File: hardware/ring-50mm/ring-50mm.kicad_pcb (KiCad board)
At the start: 2 copper layers, 50.2 x 56.6 mm, 53 parts, among them J1 Conn_01x03, J2 Conn_01x03

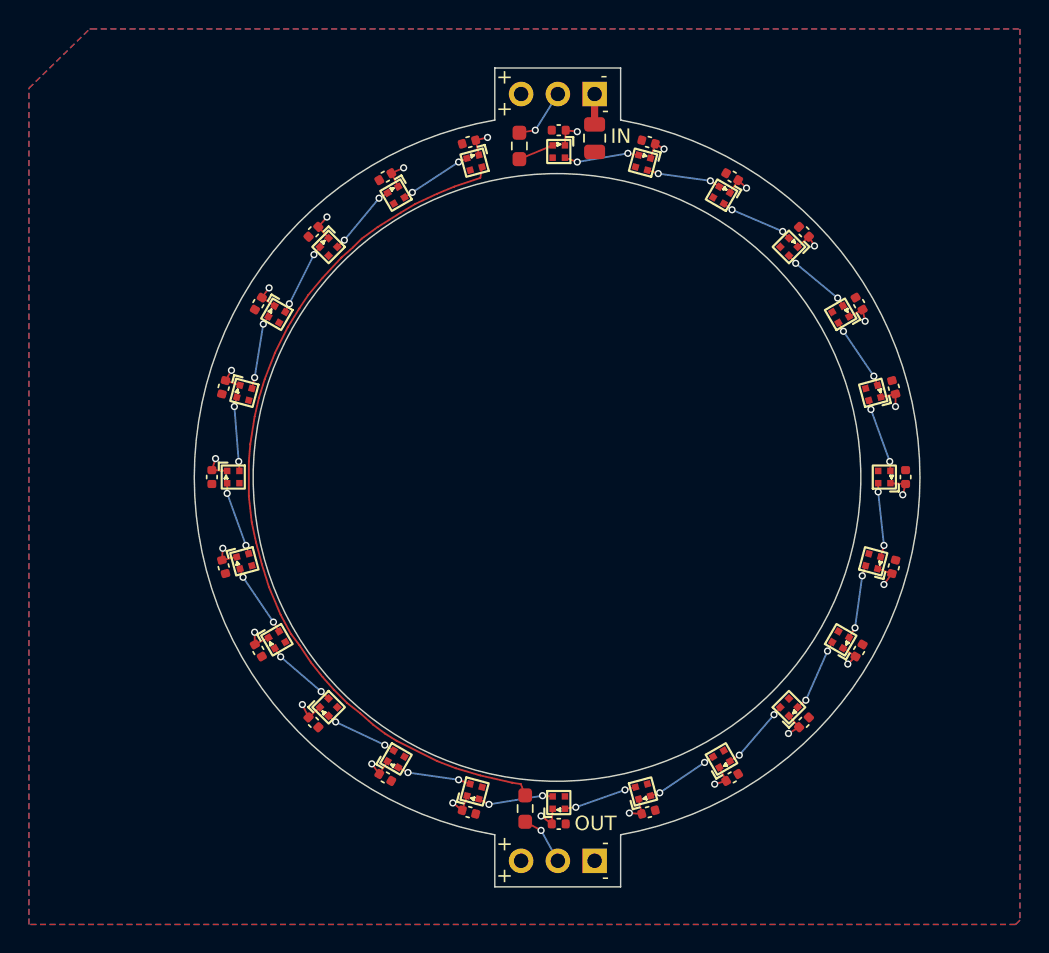
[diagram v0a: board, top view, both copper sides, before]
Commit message: Round traces and generate production files for ring-50mm
Change-Id: I082e9b078fae183d01e202b541b74c2da0abce6b
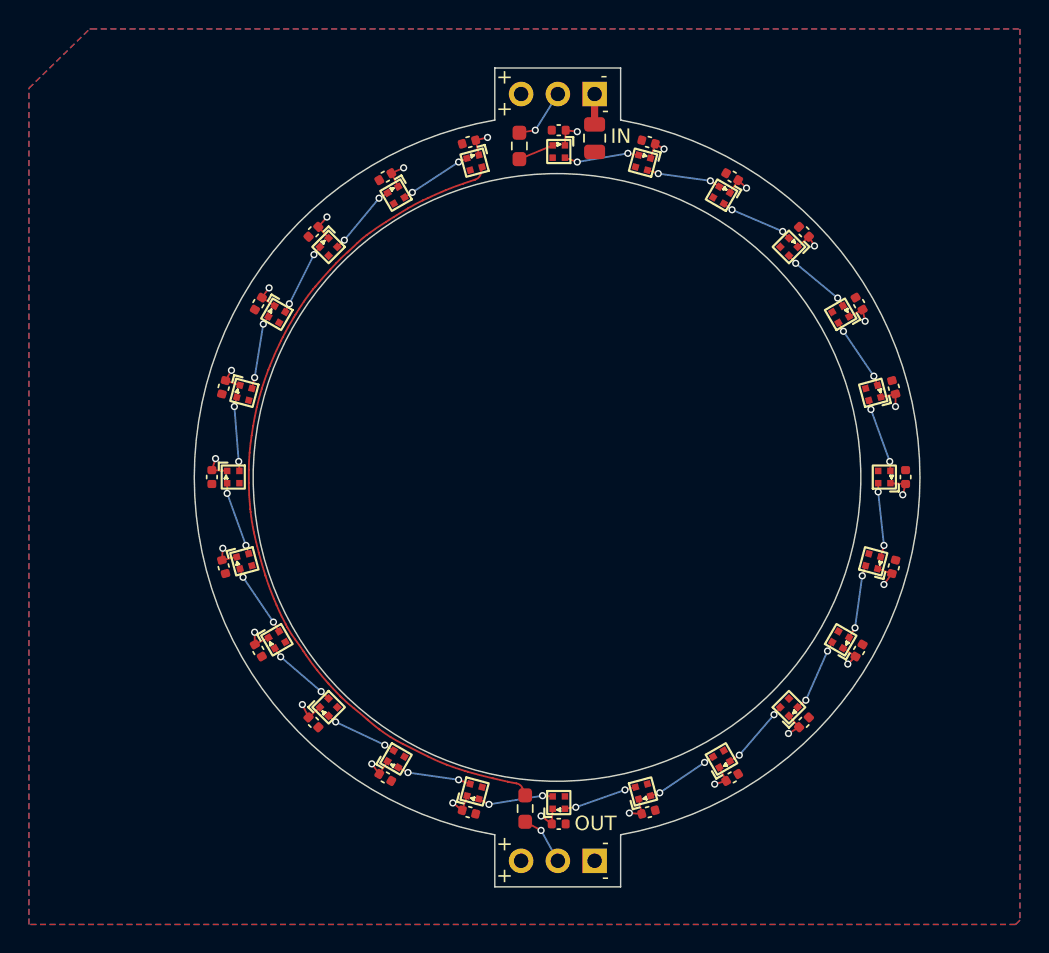
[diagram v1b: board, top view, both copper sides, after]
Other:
- board text added: "v1.0"
